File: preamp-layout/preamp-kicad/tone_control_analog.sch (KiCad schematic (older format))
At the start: 58 parts

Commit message: Added preliminary gain stage
Gain stage added with choice of 6db or 12db gain. Cleaned up Gain stage IO pins on preamp sheet. Broke out volume ctrl to its own board, updated accordingly. Minor routing changes on preamp sheet.
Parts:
- removed C? (x5): C, symbol Device:C
- removed D?: LED, symbol Device:LED
- removed J?: Conn_01x03_Female, symbol Connector:Conn_01x03_Female
- removed J?: Conn_01x03_Male, symbol Connector:Conn_01x03_Male
- removed R? (x10): 10K, symbol Device:R
- removed U? (x2): TL072, symbol Amplifier_Operational:TL072
- added C? (x5): C, symbol Device:C
- added D?: LED, symbol Device:LED
- added J?: Conn_01x03_Female, symbol Connector:Conn_01x03_Female
- added J?: Conn_01x03_Male, symbol Connector:Conn_01x03_Male
- added R? (x10): 10K, symbol Device:R
- added U? (x2): TL072, symbol Amplifier_Operational:TL072
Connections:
- net +15V: now also R?.1
- net -15V: now also R?.1
- net GNDA: now also D?.1 (K), R?.2, U?.5 (+)
- net GNDS: now also J?.3 (Pin_3), J?.3 (Pin_3)
- net IN_L: now also C?.2, J?.1 (Pin_1)
- net IN_R: now also J?.2 (Pin_2)
- net OUT_L: now also J?.1 (Pin_1), R?.1, U?.7
- net OUT_R: now also J?.2 (Pin_2), R?.1, R?.1
- net at RV?.4: now also R?.2
- net at RV?.5: now also C?.2 (x3)
- net at RV?.6: now also R?.1
- net at C?.2, R?.2, R?.2: now also R?.2, R?.2
- net at C?.2, RV?.6: now also R?.1 (x2)
- net at C?.1, RV?.4: now also R?.2 (x2)
- net at C?.1, U?.6 (-): now also C?.1, C?.1, R?.1
- net at RV?.5: now also R?.2
- net at R?.1, RV?.6: now also C?.2
- net at C?.2, R?.2, R?.2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: now also R?.2
- net at R?.2, RV?.4: now also C?.1
- net at C?.1, C?.1, R?.1: now also C?.1, U?.6 (-)
- net at C?.1: now also U?.1, U?.2 (-)
- net at D?.1 (K): now also R?.2
- new net: C?.1, R?.1, U?.3 (+)
- new net: D?.2 (A), R?.2

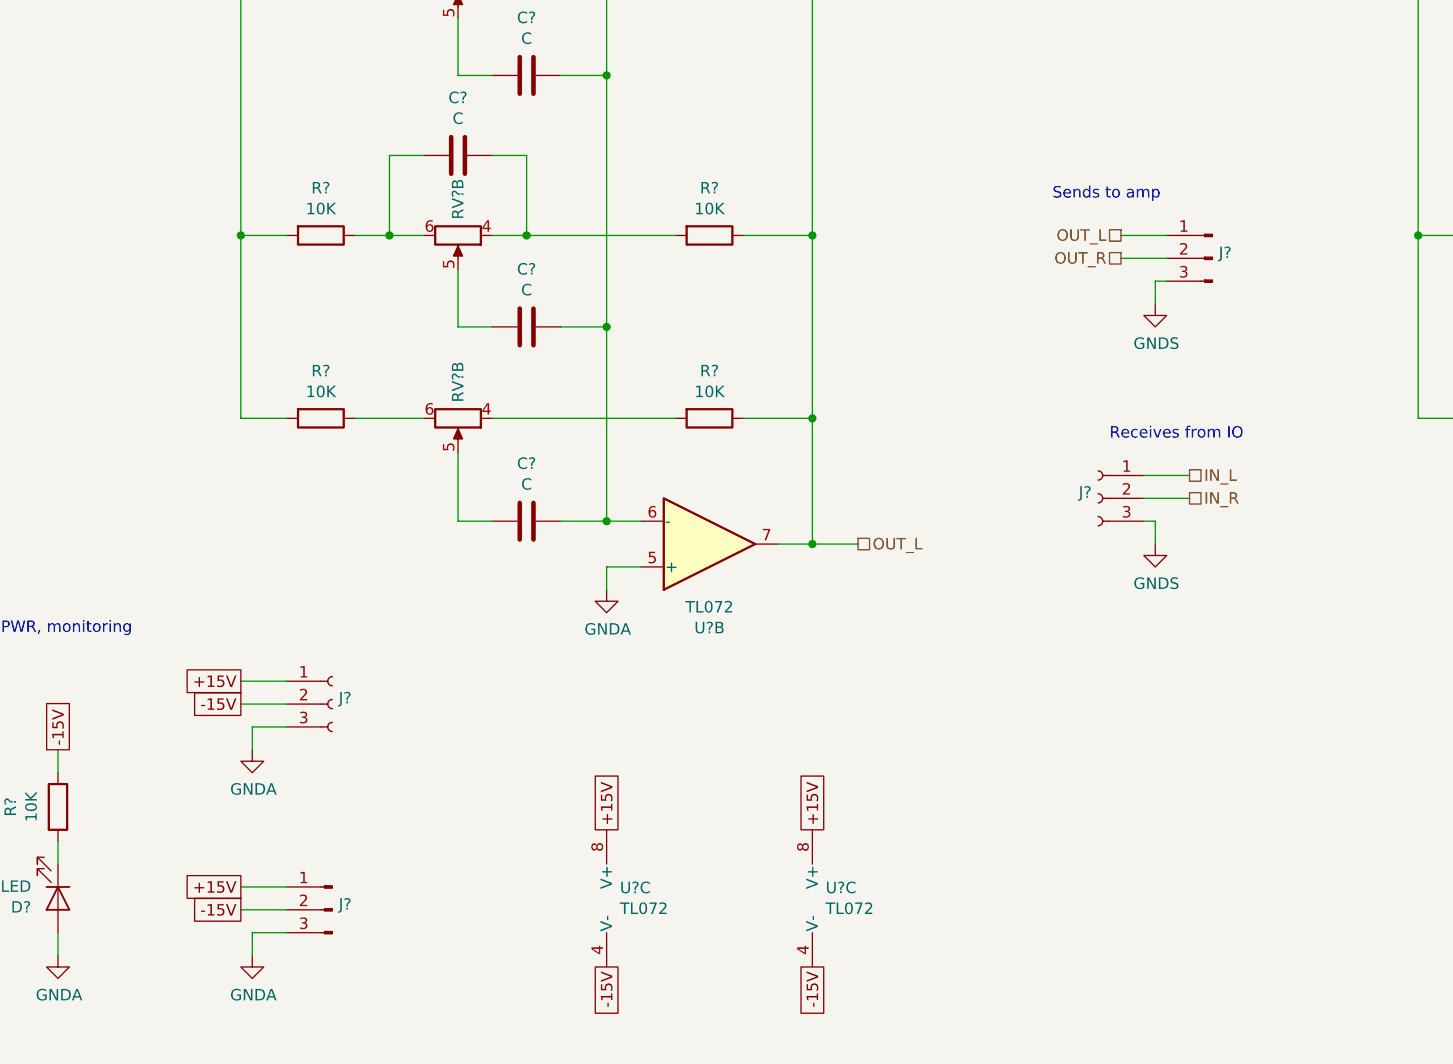
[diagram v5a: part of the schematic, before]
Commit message: Created component library, changed connector pinouts
Project library was created for this project to house custom parts, starting with Omron relay. 15V supply conn output changed so that pin 1 remains +15V, but pin 2 is now common and pin 3 is now -15V. SImilarly, 3 pin audio conn changed so that pin 2 is common and pin 3 is Right channel.

Implemented new schematic symbol for relays, general sheet cleanup. Removed MISO from IO selector board.
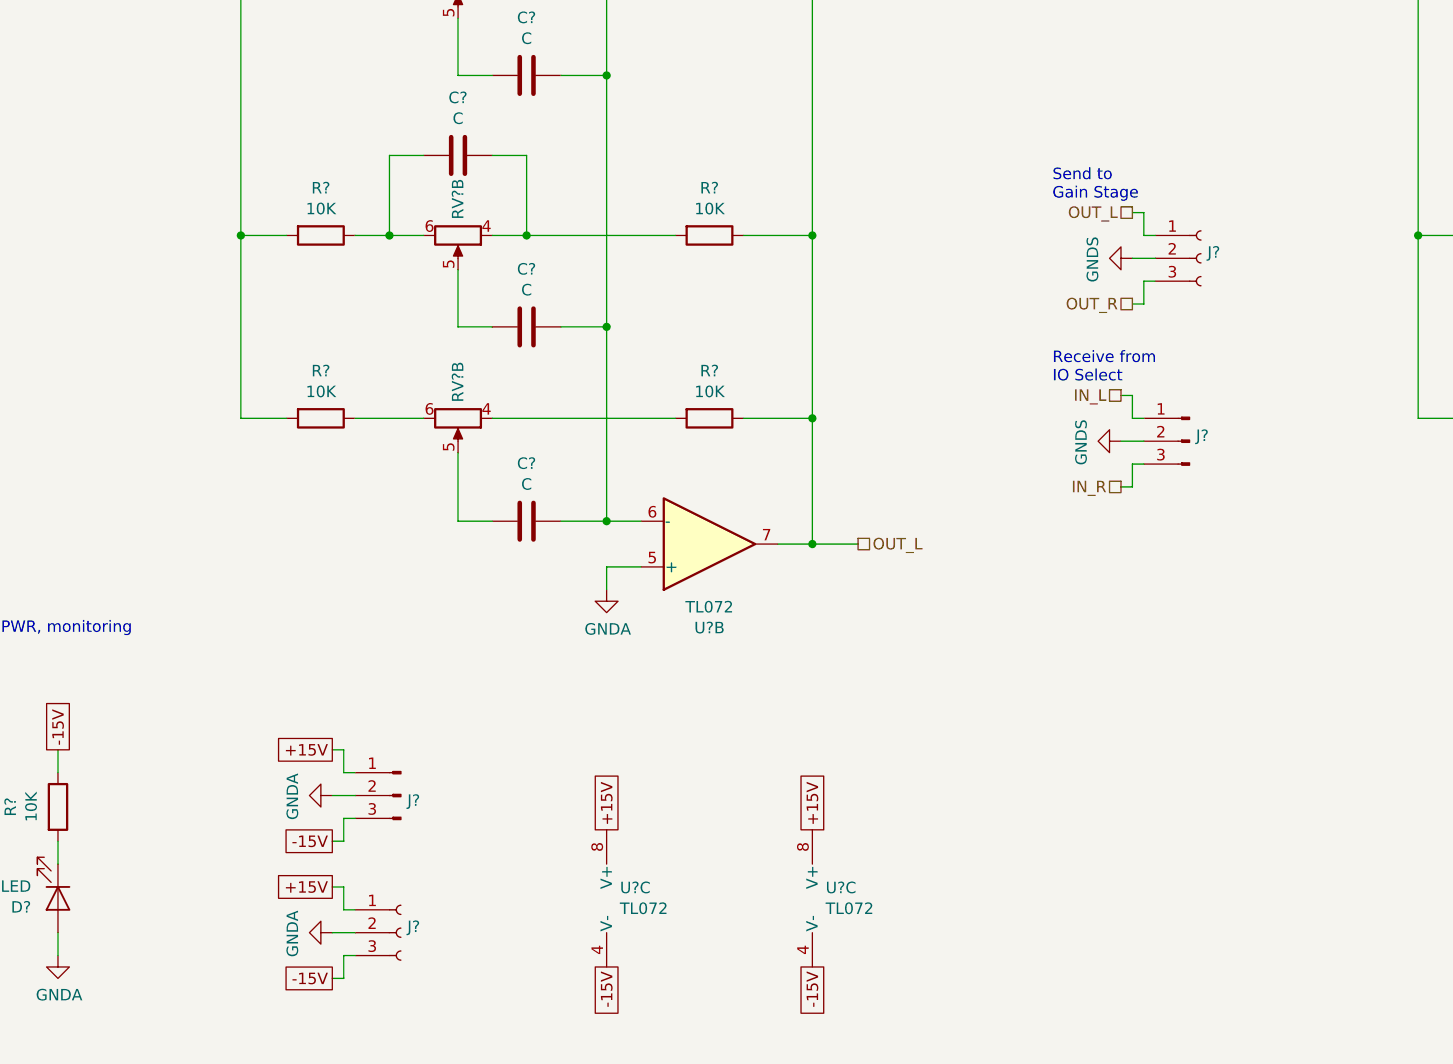
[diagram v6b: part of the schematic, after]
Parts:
- removed J? (x2): Conn_01x03_Male, symbol Connector:Conn_01x03_Male
- removed J?: Conn_01x03_Female, symbol Connector:Conn_01x03_Female
- added J? (x2): Conn_01x03_Male, symbol Connector:Conn_01x03_Male
- added J?: Conn_01x03_Female, symbol Connector:Conn_01x03_Female
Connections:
- net +15V: now also J?.1 (Pin_1), J?.1 (Pin_1)
- net -15V: now also J?.3 (Pin_3), J?.3 (Pin_3)
- net GNDA: now also J?.2 (Pin_2), J?.2 (Pin_2)
- net GNDS: now also J?.2 (Pin_2), J?.2 (Pin_2); no longer J?.3 (Pin_3)
- net IN_L: now also J?.1 (Pin_1); no longer J?.1 (Pin_1)
- net IN_R: now also J?.3 (Pin_3); no longer J?.2 (Pin_2)
- net OUT_L: now also J?.1 (Pin_1)
- net OUT_R: now also J?.3 (Pin_3)
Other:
- note added: "Receive from\nIO Select"
- note added: "Send to\nGain Stage"
- note removed: "Receives from IO"
- note removed: "Sends to amp"
- moved on the sheet: J?

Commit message: Grounds cleaned up, initial refdes numbering, error correction
GNDA, GNDS, GNDD, GND all combined to GND. No point in having separate grounds for this design.

Initial refdes numbering done using auto numbering feature. Error detection run and multple issues found which prompted Ground fix, as well as learning the disconnected pins require a 'no connection' flag to not throw an error.

Error correction also prompted the AC power connector symbol change to a plug to attempt to fix an error regarding 'driving' the circuit....more work to be done on error analysis.
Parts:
- gave numbers to parts that had none: 50
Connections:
- net GNDS is gone; now on net GND: J52.2 (Pin_2), J53.2 (Pin_2)
- net at C47.2, R78.1: now also RV6.3; no longer RV6.6
- net at C47.1, R83.2: now also RV6.1; no longer RV6.4
- net at C49.2, R80.1: now also RV7.3; no longer RV7.6
- net at C49.1, R85.2: now also RV7.1; no longer RV7.4
- net at C51.2: now also RV7.2; no longer RV7.5
- net at R82.2: now also RV6.2; no longer RV6.5
- net at C39.2, R68.1: now also RV4.3; no longer RV4.6
- net at C39.1, R73.2: now also RV4.1; no longer RV4.4
- net at R72.2: now also RV4.2; no longer RV4.5
- net at C41.2, R70.1: now also RV5.3; no longer RV5.6
- net at C41.1, R75.2: now also RV5.1; no longer RV5.4
- net at C43.2: now also RV5.2; no longer RV5.5
- net GNDA renamed GND
